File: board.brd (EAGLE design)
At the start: 67.3 x 44.4 mm, 87 parts, among them J1 AVR_SPI_PRG_6NS, U1 TPS2112A, U2 MAX1555, U3 USD-SOCKETNEW, U4 3.3V, U5 2.8V, U6 74HC595, Y1 8MHz, Y2 12.288MHz

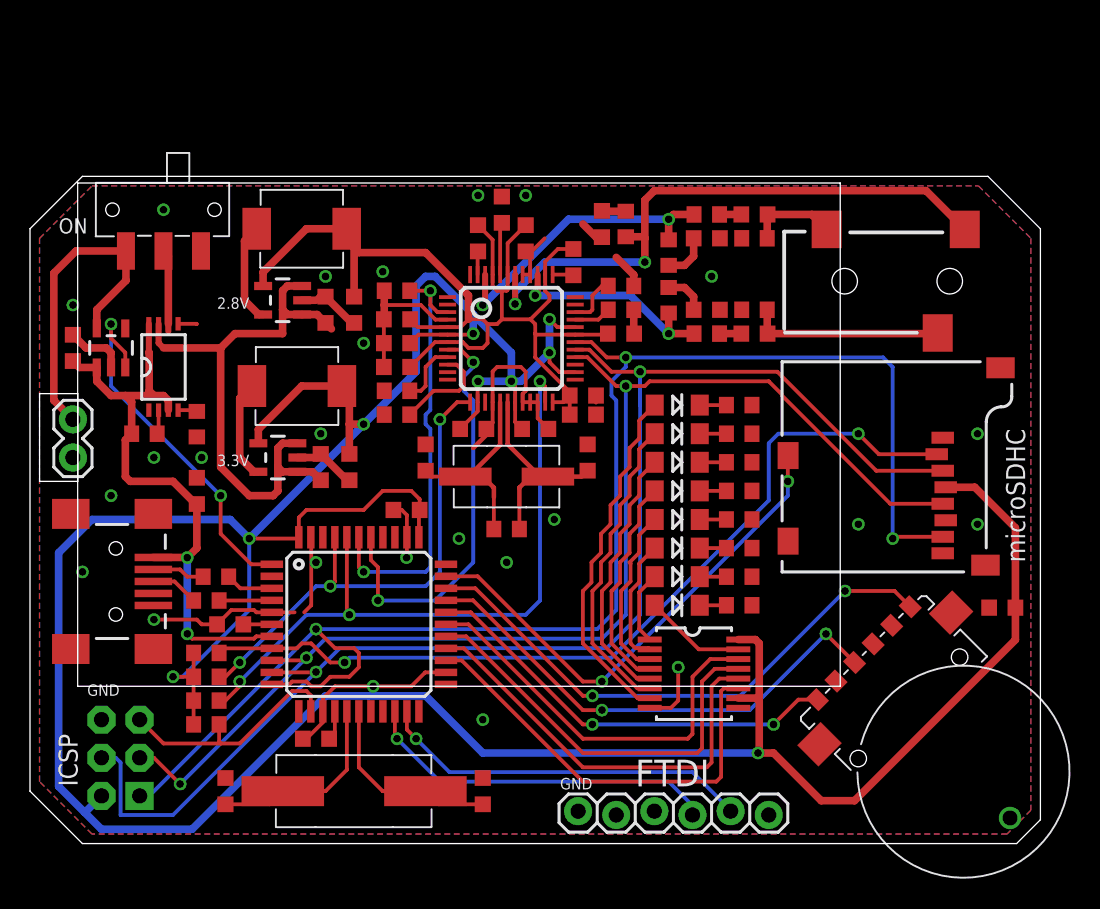
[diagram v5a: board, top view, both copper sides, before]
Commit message: Added battery sense, updated revision, and centered LEDs
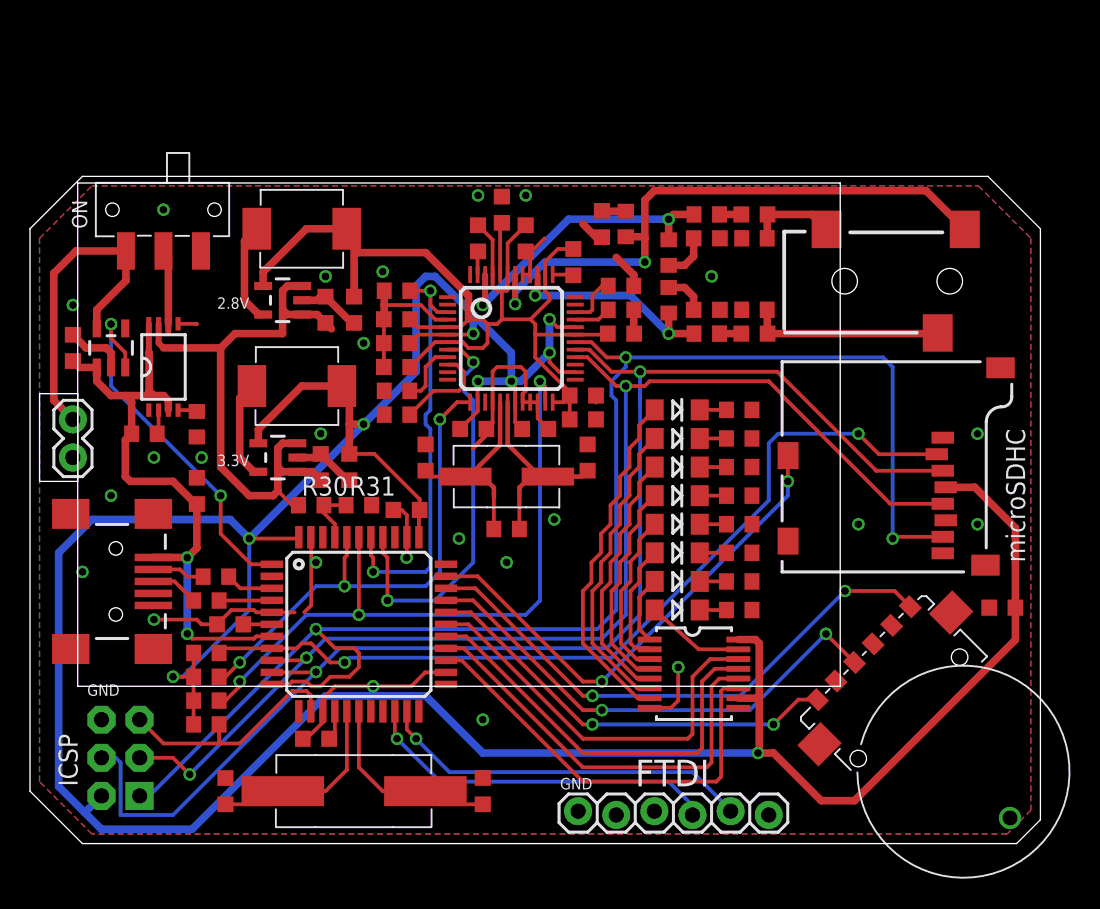
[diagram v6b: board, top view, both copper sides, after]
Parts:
- added R30, R31: 10k, rcl:R0603
- moved C17 0.32 mm to (36.2, 27.6)
- moved LED7 0.32 mm to (42.5, 26.4)
- moved R27 0.32 mm to (46.6, 26.4)
- moved LED1 0.32 mm to (42.5, 14.9)
- moved R21 0.32 mm to (46.6, 14.9)
- moved LED2 0.32 mm to (42.5, 16.8)
- moved LED3 0.32 mm to (42.5, 18.7)
- moved LED4 0.32 mm to (42.5, 20.6)
- moved LED5 0.32 mm to (42.5, 22.5)
- moved LED6 0.32 mm to (42.5, 24.4)
- moved LED8 0.32 mm to (42.5, 28.3)
- moved R22 0.32 mm to (46.6, 16.8)
- moved R23 0.32 mm to (46.6, 18.7)
- moved R24 0.32 mm to (46.6, 20.6)
- moved R25 0.32 mm to (46.6, 22.5)
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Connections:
- new net V_READ: R30.2, R31.1, U$1.41
- net GND: now also R31.2
- net MP3_DREQ: now also U$1.37; no longer U$1.38
- net MP3_XCS: now also U$1.39; no longer U$1.40
- net MP3_XDCS: now also U$1.40; no longer U$1.41
- net MP3_XRESET: now also U$1.38; no longer U$1.39
- net N$18: now also R30.1
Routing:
- net VDD: track 248.4 -> 244.0 mm
- net V_READ: track 0.00 -> 3.91 mm
- net N$18: track 38.3 -> 40.1 mm
- net MP3_XRESET: track 29.4 -> 28.7 mm
- net MP3_DREQ: track 27.7 -> 27.0 mm
- net SCK: track 84.2 -> 83.7 mm
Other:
- board text added: "0x30"
- board text added: "MJK 12/13"
- board text removed: "2.0"
- board text removed: "MJK 09/13"

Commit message: Trace cleanup
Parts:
- moved C25 2.62 mm to (28.3, 41.0), turned to 180 degrees
- moved C21 1.14 mm to (28.3, 39.1), turned to 0 degrees
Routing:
- net CVDD: track 72.1 -> 74.8 mm
- net GND: track 76.8 -> 78.4 mm, vias 24 -> 28
- net RCAP: track 3.50 -> 4.93 mm

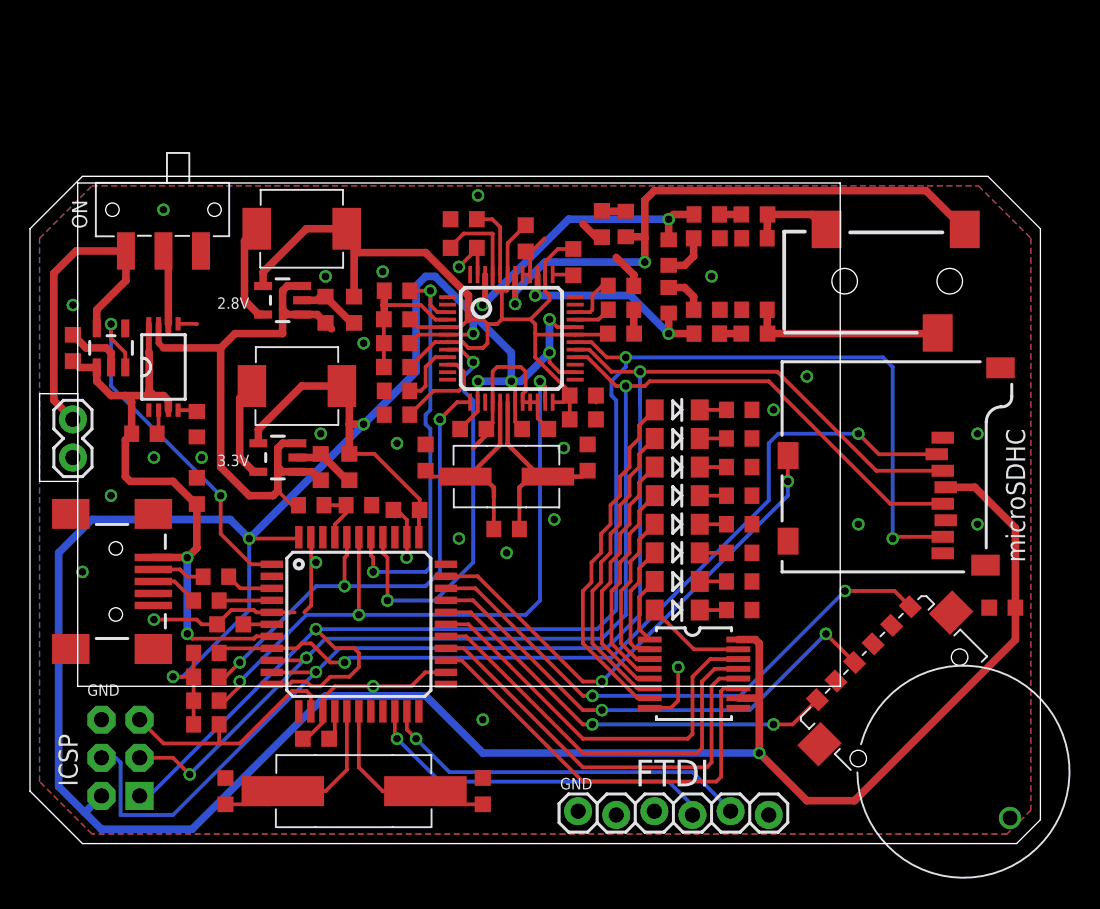
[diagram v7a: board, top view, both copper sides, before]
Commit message: A bit more space between audio jack and sdhc
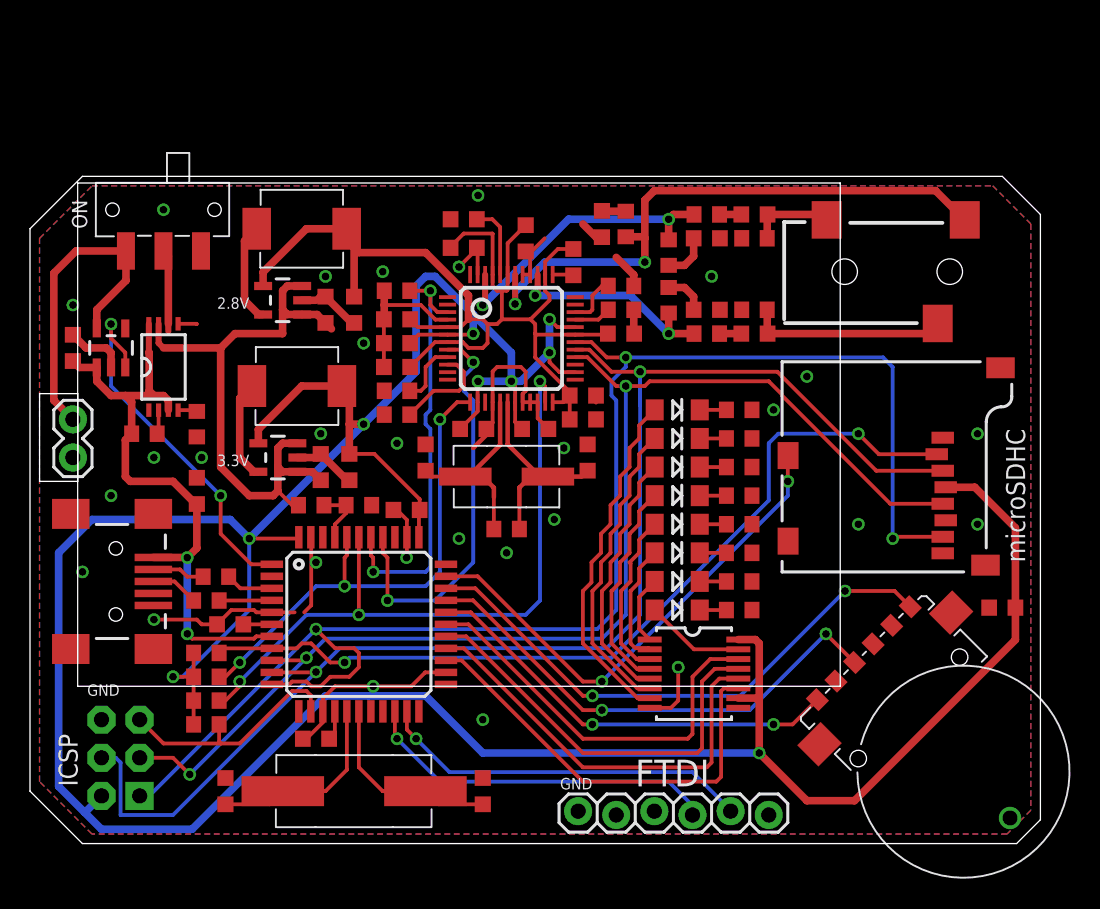
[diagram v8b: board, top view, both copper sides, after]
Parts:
- moved U7 0.64 mm to (64.1, 37.5)
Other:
- outline, holes or cut-outs redrawn
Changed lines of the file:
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@@
 <wire x1="-0.635" y1="2.8575" x2="-0.635" y2="40.3225" width="0" layer="20"/>
 <wire x1="-0.635" y1="40.3225" x2="2.8575" y2="43.815" width="0" layer="20"/>
-<wire x1="2.8575" y1="43.815" x2="63.1825" y2="43.815" width="0" layer="20"/>
-<wire x1="63.1825" y1="43.815" x2="66.675" y2="40.3225" width="0" layer="20"/>
-<wire x1="66.675" y1="40.3225" x2="66.675" y2="0.9525" width="0" layer="20"/>
+<wire x1="2.8575" y1="43.815" x2="64.135" y2="43.815" width="0" layer="20"/>
+<wire x1="64.135" y1="43.815" x2="66.675" y2="41.275" width="0" layer="20"/>
+<wire x1="66.675" y1="41.275" x2="66.675" y2="0.9525" width="0" layer="20"/>
 <wire x1="66.675" y1="0.9525" x2="65.0875" y2="-0.635" width="0" layer="20"/>
 <wire x1="65.0875" y1="-0.635" x2="2.8575" y2="-0.635" width="0" layer="20"/>
@@
 <element name="C6" library="rcl" package="C0603K" value="1u" x="2.2225" y="32.385" smashed="yes" rot="R90"/>
 <element name="S2" library="mkmp3" package="EVQ-WKA" value="EVQ-WKA" x="54.2925" y="11.43" smashed="yes" rot="R225"/>
-<element name="U7" library="mkmp3" package="AUDIO-JACK-3.5MM-SMD" value="" x="64.135" y="36.83" smashed="yes" rot="R180"/>
+<element name="U7" library="mkmp3" package="AUDIO-JACK-3.5MM-SMD" value="" x="64.135" y="37.465" smashed="yes" rot="R180"/>
 <element name="LED8" library="LilyPad-Wearables" package="LED-1206" value="" x="42.4815" y="28.2575" smashed="yes">
 <attribute name="VALUE" x="40.3115" y="25.5175" size="1.27" layer="27"/>
@@
 <vertex x="0" y="39.6875"/>
 <vertex x="3.4925" y="43.18"/>
-<vertex x="62.5475" y="43.18"/>
-<vertex x="66.04" y="39.6875"/>
+<vertex x="63.5" y="43.18"/>
+<vertex x="66.04" y="40.64"/>
 <vertex x="66.04" y="1.5875"/>
 <vertex x="64.4525" y="0"/>
@@
 <vertex x="0" y="39.6875"/>
 <vertex x="3.4925" y="43.18"/>
-<vertex x="62.5475" y="43.18"/>
-<vertex x="66.04" y="39.6875"/>
+<vertex x="63.5" y="43.18"/>
+<vertex x="66.04" y="40.64"/>
 <vertex x="66.04" y="1.5875"/>
 <vertex x="64.4525" y="0"/>
@@
 <via x="40.3225" y="38.1" extent="1-16" drill="0.5"/>
 <wire x1="40.3225" y1="38.1" x2="33.655" y2="38.1" width="0.508" layer="16"/>
-<wire x1="40.9575" y1="42.8625" x2="59.0525" y2="42.8625" width="0.508" layer="1"/>
-<wire x1="59.0525" y1="42.8625" x2="61.635" y2="40.28" width="0.508" layer="1"/>
+<wire x1="40.9575" y1="42.8625" x2="59.6875" y2="42.8625" width="0.508" layer="1"/>
+<wire x1="59.6875" y1="42.8625" x2="61.635" y2="40.915" width="0.508" layer="1"/>
 <wire x1="40.3225" y1="38.1" x2="40.3225" y2="39.6875" width="0.508" layer="1"/>
 <wire x1="40.3225" y1="39.6875" x2="40.3225" y2="42.2275" width="0.508" layer="1"/>
@@
 <wire x1="48.475" y1="34.925" x2="48.475" y2="33.3625" width="0.508" layer="1"/>
 <wire x1="48.475" y1="33.3625" x2="48.5" y2="33.3375" width="0.508" layer="1"/>
-<wire x1="48.5" y1="33.3375" x2="59.7925" y2="33.3375" width="0.508" layer="1"/>
-<wire x1="59.7925" y1="33.3375" x2="59.835" y2="33.38" width="0.508" layer="1"/>
+<wire x1="48.5" y1="33.3375" x2="59.1575" y2="33.3375" width="0.508" layer="1"/>
+<wire x1="59.1575" y1="33.3375" x2="59.835" y2="34.015" width="0.508" layer="1"/>
 </signal>
 <signal name="N$13">
@@
 <wire x1="48.475" y1="39.6875" x2="48.475" y2="41.25" width="0.508" layer="1"/>
 <wire x1="48.475" y1="41.25" x2="48.5" y2="41.275" width="0.508" layer="1"/>
-<wire x1="48.5" y1="41.275" x2="51.44" y2="41.275" width="0.508" layer="1"/>
-<wire x1="51.44" y1="41.275" x2="52.435" y2="40.28" width="0.508" layer="1"/>
+<wire x1="48.5" y1="41.275" x2="52.075" y2="41.275" width="0.508" layer="1"/>
+<wire x1="52.075" y1="41.275" x2="52.435" y2="40.915" width="0.508" layer="1"/>
 </signal>
 <signal name="N$1">
